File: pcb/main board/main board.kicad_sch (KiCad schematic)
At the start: 32 parts, among them J10 12V Battery, J11 BAU, J12 Servo 4 Conn, J13 Servo 1 Conn, J14 Servo 2 Conn, J15 Servo 3 Conn, J16 Servo 5 Conn, J17 Servo 6 Conn, J18 Servo 7 Conn, J19 Servo 8 Conn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

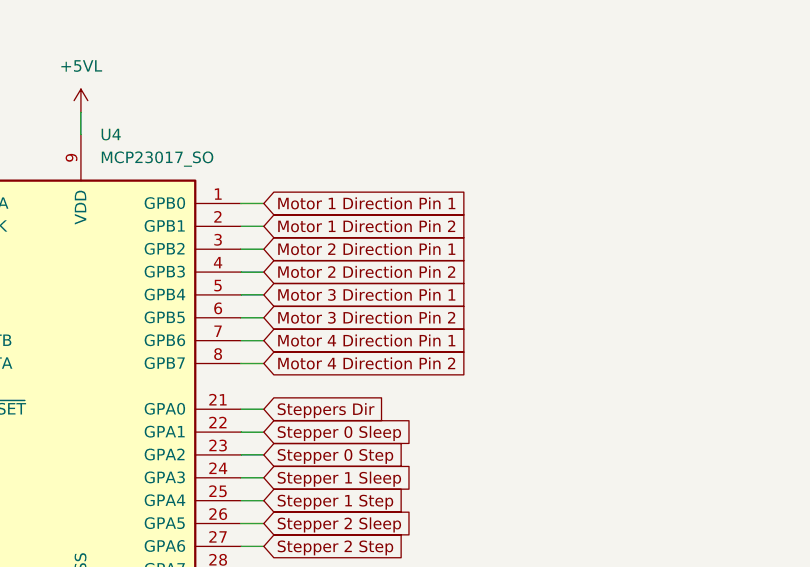
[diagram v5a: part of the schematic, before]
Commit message: Finished wiring 5VP, created mass plane and started to wire motor drivers.
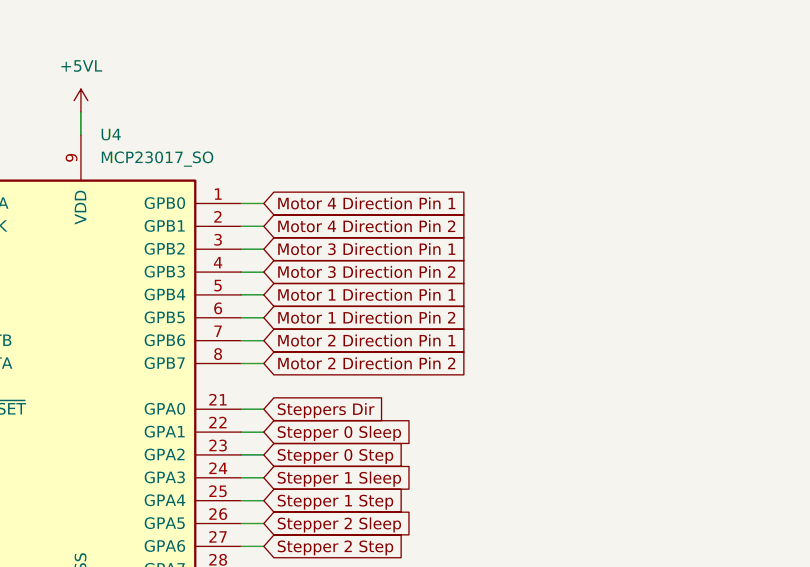
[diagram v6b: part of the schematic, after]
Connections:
- net Motor 1 Direction Pin 1: now also U4.5 (GPB4); no longer U4.1 (GPB0)
- net Motor 1 Direction Pin 2: now also U4.6 (GPB5); no longer U4.2 (GPB1)
- net Motor 2 Direction Pin 1: now also U4.7 (GPB6); no longer U4.3 (GPB2)
- net Motor 2 Direction Pin 2: now also U4.8 (GPB7); no longer U4.4 (GPB3)
- net Motor 3 Direction Pin 1: now also U4.3 (GPB2); no longer U4.5 (GPB4)
- net Motor 3 Direction Pin 2: now also U4.4 (GPB3); no longer U4.6 (GPB5)
- net Motor 4 Direction Pin 1: now also U4.1 (GPB0); no longer U4.7 (GPB6)
- net Motor 4 Direction Pin 2: now also U4.2 (GPB1); no longer U4.8 (GPB7)

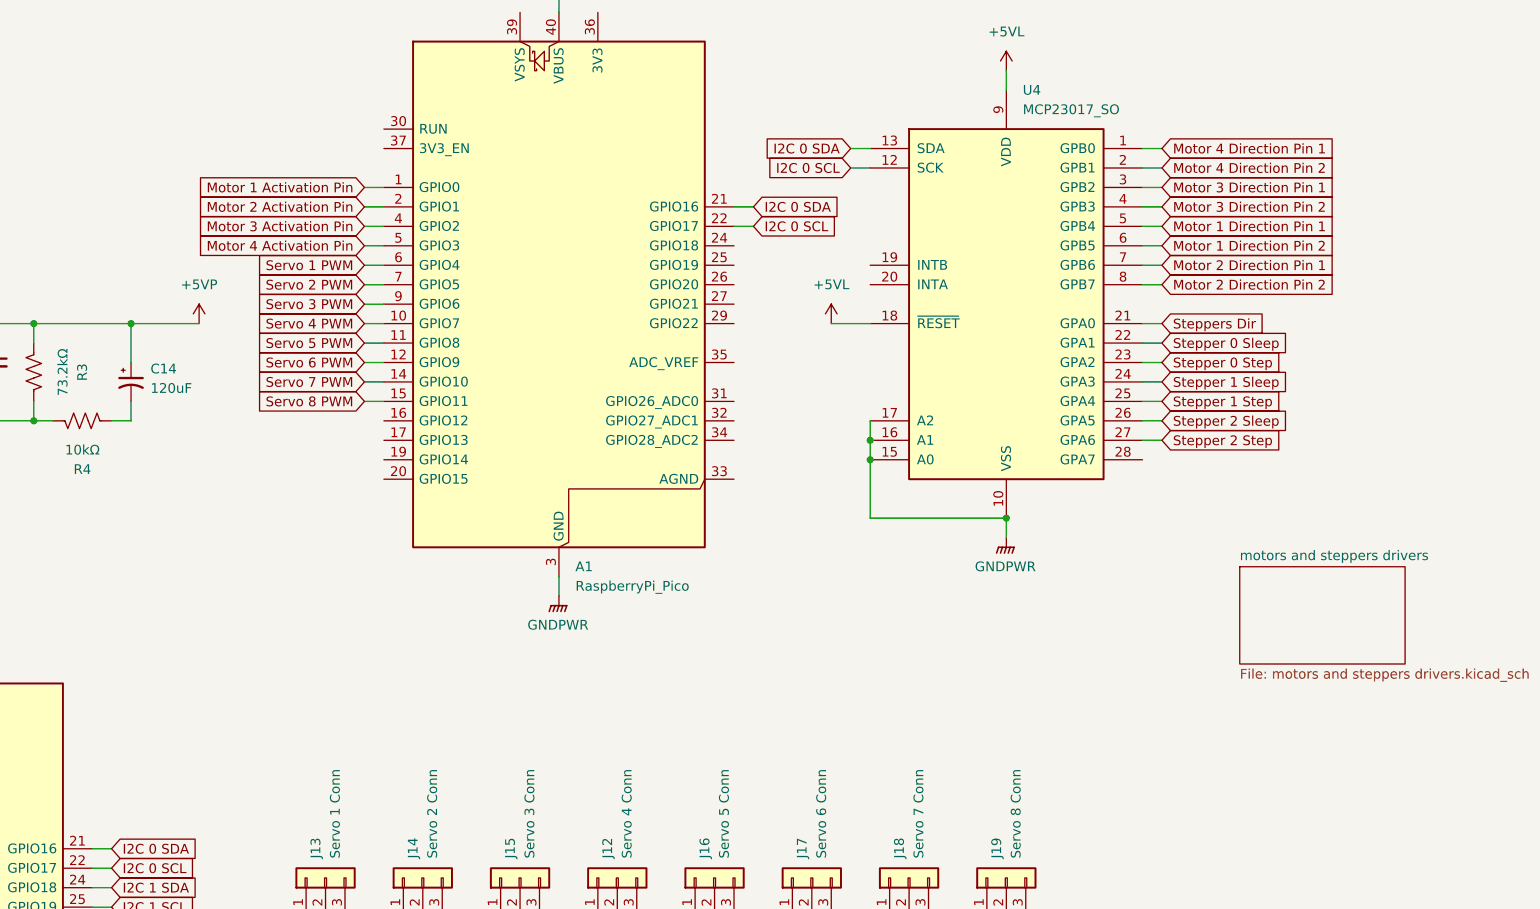
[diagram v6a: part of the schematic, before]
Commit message: Almost finished wiring motors drivers and continued connecting the rest. Also modified the LM2596S Module to put a hole in the board
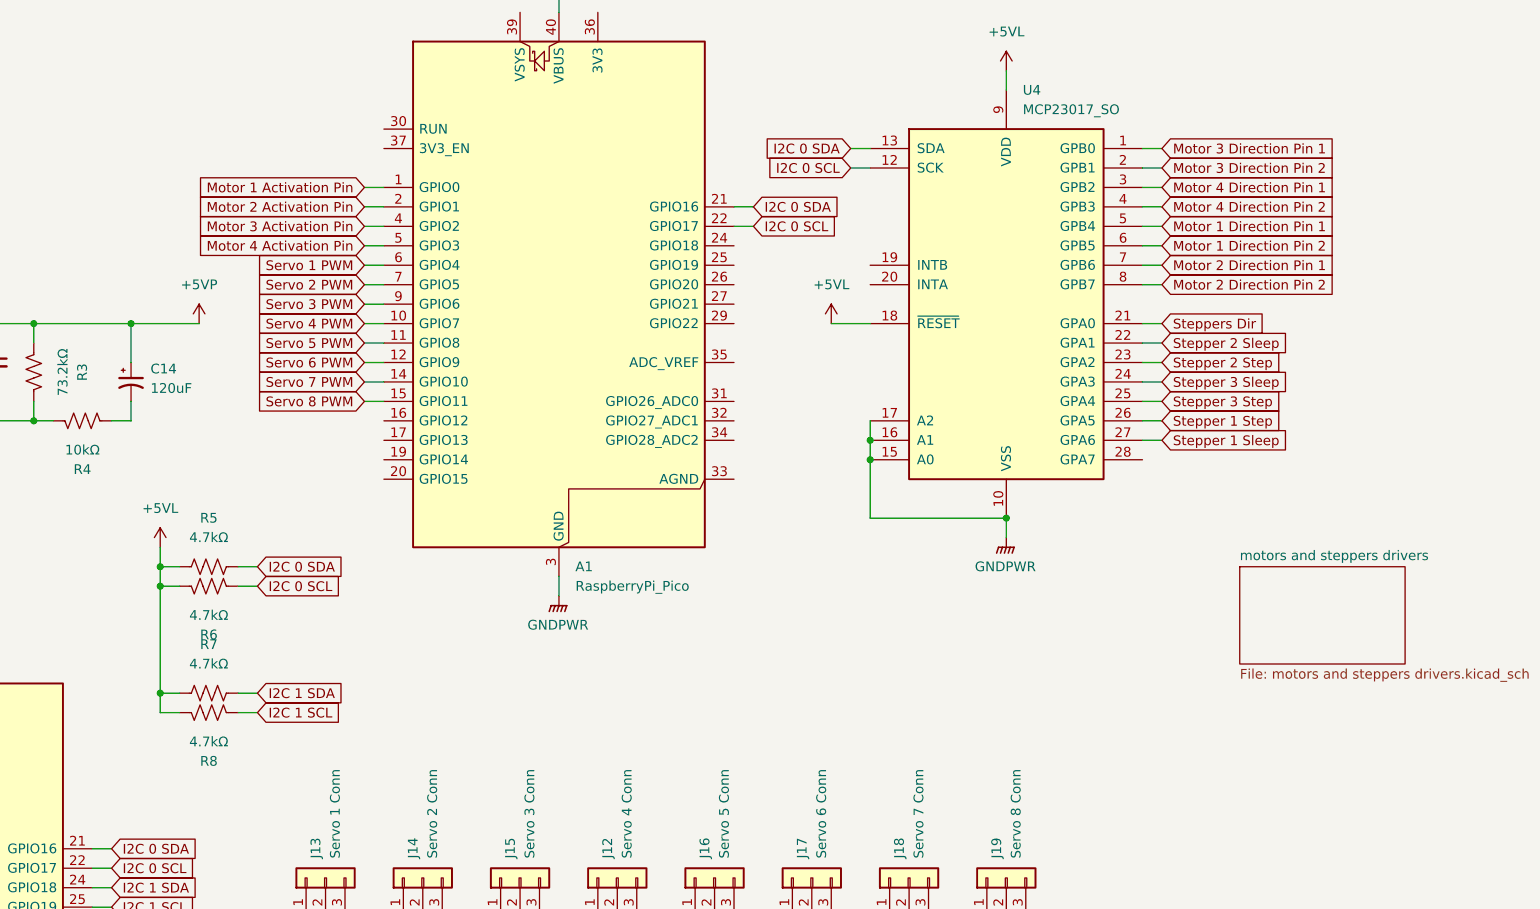
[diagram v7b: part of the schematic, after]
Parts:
- added R5, R6, R7, R8: 4.7kΩ, Resistor_THT:R_Axial_DIN0207_L6.3mm_D2.5mm_P10.16mm_Horizontal, symbol Device:R_US
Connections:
- net Stepper 0 Sleep is gone; now on net Stepper 2 Sleep: U4.22 (GPA1)
- net Stepper 0 Step is gone; now on net Stepper 2 Step: U4.23 (GPA2)
- net +5VL: now also R5.1, R6.1, R7.1, R8.1
- net I2C 0 SCL: now also R6.2
- net I2C 0 SDA: now also R5.2
- net I2C 1 SCL: now also R8.2
- net I2C 1 SDA: now also R7.2
- net Motor 3 Direction Pin 1: now also U4.1 (GPB0); no longer U4.3 (GPB2)
- net Motor 3 Direction Pin 2: now also U4.2 (GPB1); no longer U4.4 (GPB3)
- net Motor 4 Direction Pin 1: now also U4.3 (GPB2); no longer U4.1 (GPB0)
- net Motor 4 Direction Pin 2: now also U4.4 (GPB3); no longer U4.2 (GPB1)
- net Stepper 1 Sleep: now also U4.27 (GPA6); no longer U4.24 (GPA3)
- net Stepper 1 Step: now also U4.26 (GPA5); no longer U4.25 (GPA4)
- net Stepper 2 Sleep: no longer U4.26 (GPA5)
- net Stepper 2 Step: no longer U4.27 (GPA6)
- new net Stepper 3 Sleep: U4.24 (GPA3)
- new net Stepper 3 Step: U4.25 (GPA4)

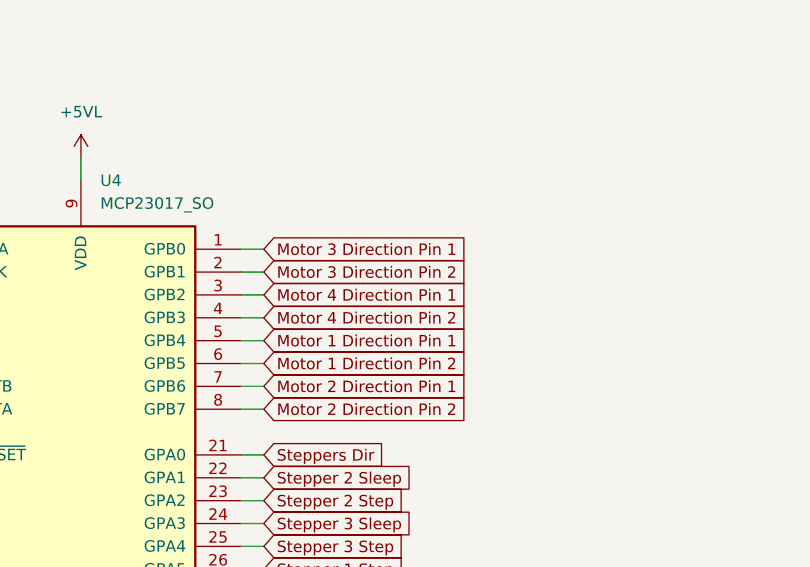
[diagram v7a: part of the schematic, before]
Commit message: Changed largeur of pistes and finished rewiring DC motors drivers
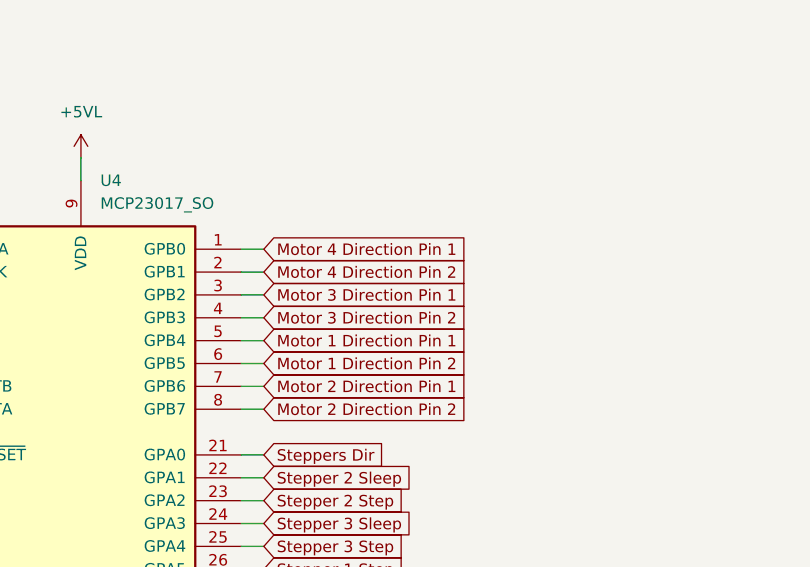
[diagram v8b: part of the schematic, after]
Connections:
- net Motor 3 Direction Pin 1: now also U4.3 (GPB2); no longer U4.1 (GPB0)
- net Motor 3 Direction Pin 2: now also U4.4 (GPB3); no longer U4.2 (GPB1)
- net Motor 4 Direction Pin 1: now also U4.1 (GPB0); no longer U4.3 (GPB2)
- net Motor 4 Direction Pin 2: now also U4.2 (GPB1); no longer U4.4 (GPB3)
